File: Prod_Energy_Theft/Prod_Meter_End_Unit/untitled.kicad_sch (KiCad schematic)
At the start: 11 parts, among them J5 Screw_Terminal_01x02, J9 Screw_Terminal_01x02, K2 Relay_DPST_Latching_2coil, Q3 AO3400A, Q4 AO3400A

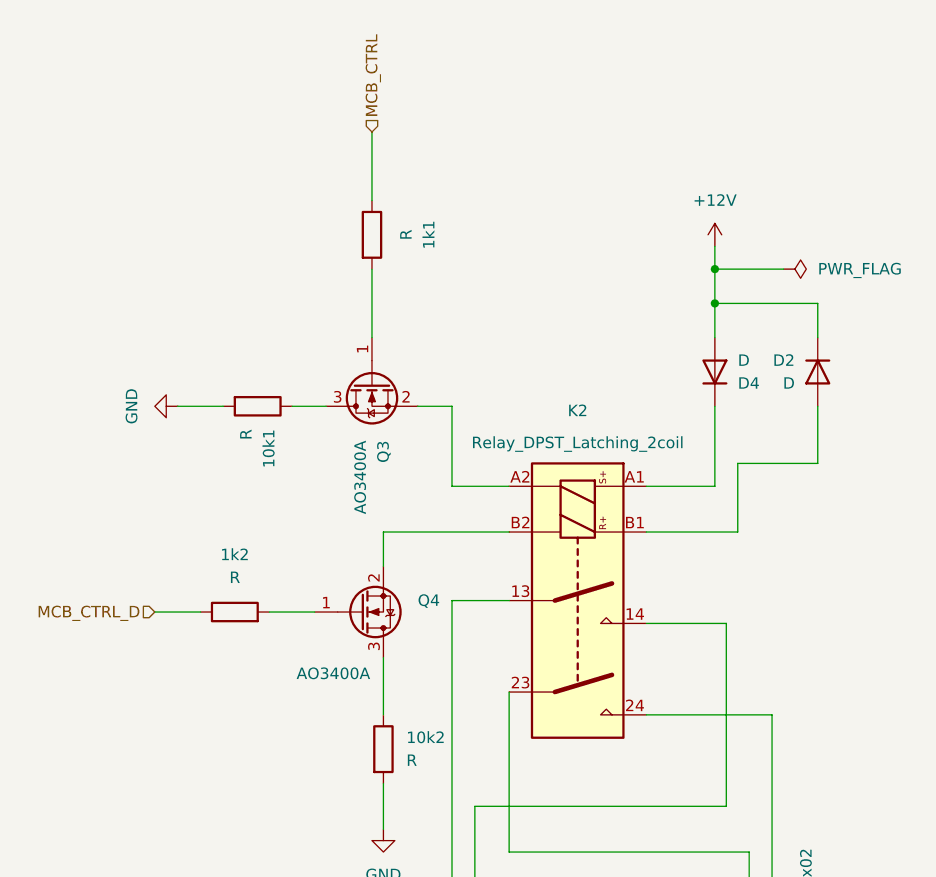
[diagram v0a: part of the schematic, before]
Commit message: Chnages in power and ADE7816
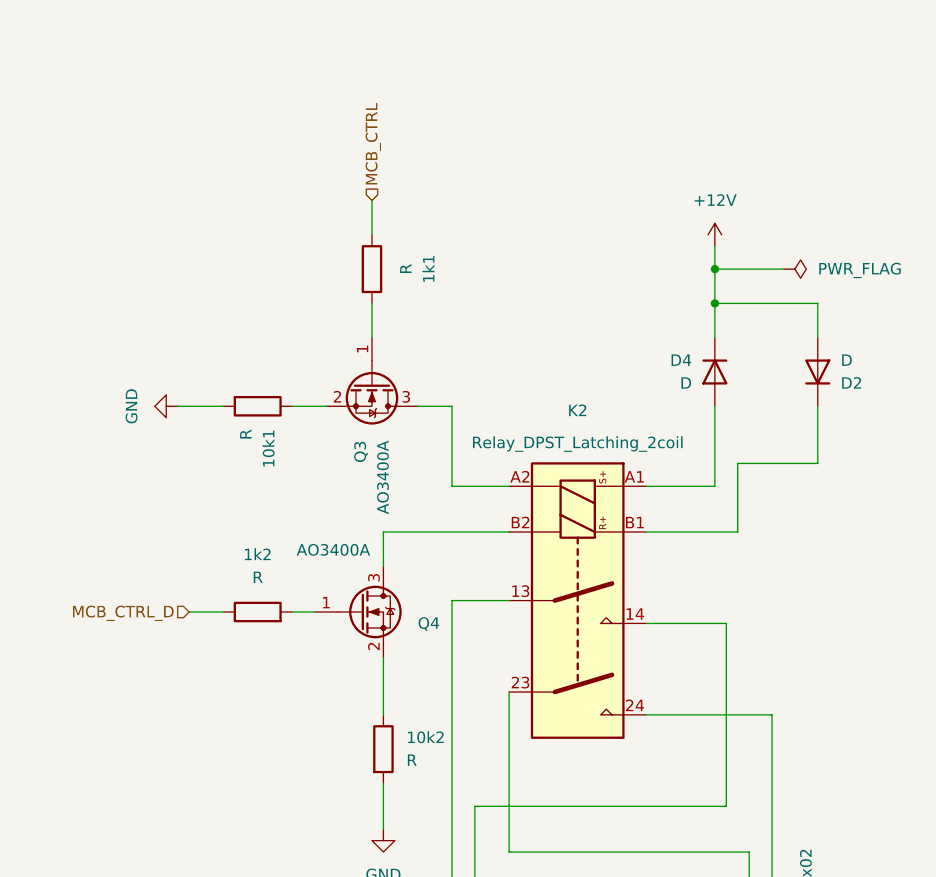
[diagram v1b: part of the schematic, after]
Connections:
- net +12V: now also D2.2 (A), D4.1 (K); no longer D2.1 (K), D4.2 (A)
- net at K2.A1: now also D4.2 (A); no longer D4.1 (K)
- net at K2.A2: now also Q3.3 (D); no longer Q3.2 (S)
- net at K2.B1: now also D2.1 (K); no longer D2.2 (A)
- net at K2.B2: now also Q4.3 (D); no longer Q4.2 (S)
- net at 10k2.1: now also Q4.2 (S); no longer Q4.3 (D)
- net at 10k1.1: now also Q3.2 (S); no longer Q3.3 (D)
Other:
- moved on the sheet: 1k1, 1k2, D2, D4, Q3
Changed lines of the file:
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@@
 	(wire
 		(pts
-			(xy 116.84 72.39) (xy 116.84 80.01)
+			(xy 116.84 76.2) (xy 116.84 80.01)
 		)
 		(stroke
@@
 	(wire
 		(pts
-			(xy 111.76 87.63) (xy 107.95 87.63)
-		)
-		(stroke
-			(width 0)
-			(type default)
-		)
-	)
-	(wire
-		(pts
-			(xy 105.41 110.49) (xy 110.49 110.49)
+			(xy 107.95 110.49) (xy 110.49 110.49)
 		)
 		(stroke
@@
 	(wire
 		(pts
+			(xy 118.11 115.57) (xy 118.11 121.92)
+		)
+		(stroke
+			(width 0)
+			(type default)
+		)
+	)
+	(wire
+		(pts
 			(xy 154.94 69.85) (xy 154.94 72.39)
 		)
@@
 	(wire
 		(pts
-			(xy 118.11 121.92) (xy 118.11 115.57)
-		)
-		(stroke
-			(width 0)
-			(type default)
-		)
-	)
-	(wire
-		(pts
 			(xy 100.33 87.63) (xy 95.25 87.63)
 		)
@@
 	(wire
 		(pts
-			(xy 116.84 57.15) (xy 116.84 64.77)
+			(xy 116.84 64.77) (xy 116.84 68.58)
 		)
 		(stroke
@@
 	(wire
 		(pts
+			(xy 107.95 87.63) (xy 111.76 87.63)
+		)
+		(stroke
+			(width 0)
+			(type default)
+		)
+	)
+	(wire
+		(pts
 			(xy 147.32 121.92) (xy 161.29 121.92)
 		)
@@
 	(wire
 		(pts
-			(xy 92.71 110.49) (xy 97.79 110.49)
+			(xy 96.52 110.49) (xy 100.33 110.49)
 		)
 		(stroke
@@
 	(wire
 		(pts
+			(xy 147.32 96.52) (xy 154.94 96.52)
+		)
+		(stroke
+			(width 0)
+			(type default)
+		)
+	)
+	(wire
+		(pts
+			(xy 154.94 87.63) (xy 154.94 96.52)
+		)
+		(stroke
+			(width 0)
+			(type default)
+		)
+	)
+	(wire
+		(pts
+			(xy 132.08 109.22) (xy 125.73 109.22)
+		)
+		(stroke
+			(width 0)
+			(type default)
+		)
+	)
+	(wire
+		(pts
+			(xy 166.37 93.98) (xy 166.37 87.63)
+		)
+		(stroke
+			(width 0)
+			(type default)
+		)
+	)
+	(wire
+		(pts
 			(xy 121.92 87.63) (xy 125.73 87.63)
-		)
-		(stroke
-			(width 0)
-			(type default)
-		)
-	)
-	(wire
-		(pts
-			(xy 147.32 96.52) (xy 154.94 96.52)
-		)
-		(stroke
-			(width 0)
-			(type default)
-		)
-	)
-	(wire
-		(pts
-			(xy 154.94 87.63) (xy 154.94 96.52)
-		)
-		(stroke
-			(width 0)
-			(type default)
-		)
-	)
-	(wire
-		(pts
-			(xy 132.08 109.22) (xy 125.73 109.22)
-		)
-		(stroke
-			(width 0)
-			(type default)
-		)
-	)
-	(wire
-		(pts
-			(xy 166.37 93.98) (xy 166.37 87.63)
 		)
 		(stroke
@@
 	(hierarchical_label "MCB_CTRL"
 		(shape input)
-		(at 116.84 57.15 90)
+		(at 116.84 64.77 90)
 		(effects
 			(font
@@
 	(hierarchical_label "MCB_CTRL_D"
 		(shape input)
-		(at 92.71 110.49 180)
+		(at 96.52 110.49 180)
 		(effects
 			(font
@@
 	(symbol
 		(lib_id "Device:D")
-		(at 154.94 83.82 270)
+		(at 154.94 83.82 90)
 		(mirror x)
 		(unit 1)
@@
 		(dnp no)
 		(property "Reference" "D4"
-			(at 157.48 85.0901 90)
+			(at 152.4 82.5499 90)
 			(effects
 				(font
@@
 		)
 		(property "Value" "D"
-			(at 157.48 82.5501 90)
+			(at 152.4 85.0899 90)
 			(effects
 				(font
@@
 	(symbol
 		(lib_id "Device:R")
-		(at 116.84 68.58 0)
+		(at 116.84 72.39 0)
 		(unit 1)
 		(exclude_from_sim no)
@@
 		(fields_autoplaced yes)
 		(property "Reference" "1k1"
-			(at 123.19 68.58 90)
+			(at 123.19 72.39 90)
 			(effects
 				(font
@@
 		)
 		(property "Value" "R"
-			(at 120.65 68.58 90)
+			(at 120.65 72.39 90)
 			(effects
 				(font
@@
 		)
 		(property "Footprint" "Resistor_SMD:R_0805_2012Metric"
-			(at 115.062 68.58 90)
+			(at 115.062 72.39 90)
 			(effects
 				(font
@@
 		)
 		(property "Datasheet" "~"
-			(at 116.84 68.58 0)
+			(at 116.84 72.39 0)
 			(effects
 				(font
@@
 		)
 		(property "Description" "Resistor"
-			(at 116.84 68.58 0)
+			(at 116.84 72.39 0)
 			(effects
 				(font
@@
 		(lib_id "Transistor_FET:AO3400A")
 		(at 115.57 110.49 0)
-		(mirror x)
 		(unit 1)
 		(exclude_from_sim no)
@@
 		(dnp no)
 		(property "Reference" "Q4"
-			(at 121.92 109.2199 0)
+			(at 121.92 111.7601 0)
 			(effects
 				(font
@@
 		)
 		(property "Value" "AO3400A"
-			(at 108.458 117.348 0)
+			(at 108.458 103.632 0)
 			(effects
 				(font
@@
 		)
 		(property "Footprint" "Package_TO_SOT_SMD:SOT-23"
-			(at 120.65 108.585 0)
+			(at 120.65 112.395 0)
 			(effects
 				(font
@@
 		)
 		(property "Datasheet" "http://www.aosmd.com/pdfs/datasheet/AO3400A.pdf"
-			(at 120.65 106.68 0)
+			(at 120.65 114.3 0)
 			(effects
 				(font
@@
 	(symbol
 		(lib_id "Transistor_FET:AO3400A")
-		(at 116.84 85.09 90)
-		(mirror x)
+		(at 116.84 85.09 270)
 		(unit 1)
 		(exclude_from_sim no)
@@
 		(dnp no)
 		(property "Reference" "Q3"
-			(at 118.1101 91.44 0)
+			(at 115.5699 91.44 0)
 			(effects
 				(font
@@
 		)
 		(property "Value" "AO3400A"
-			(at 115.5701 91.44 0)
+			(at 118.1099 91.44 0)
 			(effects
 				(font
@@
 		)
 		(property "Footprint" "Package_TO_SOT_SMD:SOT-23"
-			(at 118.745 90.17 0)
+			(at 114.935 90.17 0)
 			(effects
 				(font
@@
 		)
 		(property "Datasheet" "http://www.aosmd.com/pdfs/datasheet/AO3400A.pdf"
-			(at 120.65 90.17 0)
+			(at 113.03 90.17 0)
 			(effects
 				(font
@@
 	(symbol
 		(lib_id "Device:R")
-		(at 101.6 110.49 90)
+		(at 104.14 110.49 90)
 		(unit 1)
 		(exclude_from_sim no)
@@
 		(fields_autoplaced yes)
 		(property "Reference" "1k2"
-			(at 101.6 104.14 90)
+			(at 104.14 104.14 90)
 			(effects
 				(font
@@
 		)
 		(property "Value" "R"
-			(at 101.6 106.68 90)
+			(at 104.14 106.68 90)
 			(effects
 				(font
@@
 		)
 		(property "Footprint" "Resistor_SMD:R_0805_2012Metric"
-			(at 101.6 112.268 90)
+			(at 104.14 112.268 90)
 			(effects
 				(font
@@
 		)
 		(property "Datasheet" "~"
-			(at 101.6 110.49 0)
+			(at 104.14 110.49 0)
 			(effects
 				(font
@@
 		)
 		(property "Description" "Resistor"
-			(at 101.6 110.49 0)
+			(at 104.14 110.49 0)
 			(effects
 				(font
@@
 	(symbol
 		(lib_id "Device:D")
-		(at 166.37 83.82 90)
+		(at 166.37 83.82 270)
 		(mirror x)
 		(unit 1)
@@
 		(dnp no)
 		(property "Reference" "D2"
-			(at 163.83 82.5499 90)
+			(at 168.91 85.0901 90)
 			(effects
 				(font
@@
 		)
 		(property "Value" "D"
-			(at 163.83 85.0899 90)
-			(effects
-				(font
+			(at 168.91 82.5501 90)
+			(effects
+				(font

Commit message: PCB
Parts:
- removed 10k1, 10k2, 1k1, 1k2: R, Resistor_SMD:R_0805_2012Metric, symbol Device:R
- removed D2, D4: D, Diode_SMD:D_SOD-123, symbol Device:D
- removed J5, J9: Screw_Terminal_01x02, TerminalBlock_Phoenix:TerminalBlock_Phoenix_PTSM-0,5-2-2,5-V-SMD_1x02-1MP_P2.50mm_Vertical, symbol Connector:Screw_Terminal_01x02
- removed K2: Relay_DPST_Latching_2coil, symbol Relay:Relay_DPST_Latching_2coil
- removed Q3, Q4: AO3400A, Package_TO_SOT_SMD:SOT-23, symbol Transistor_FET:AO3400A
- added 10k3, 10k4, 1k3, 1k4: R, Resistor_SMD:R_0805_2012Metric, symbol Device:R
- added C3: 100uf, Capacitor_SMD:C_0805_2012Metric, symbol Device:C
- added D11, D12: D, Diode_SMD:D_SOD-123, symbol Device:D
- added J12, J13: Screw_Terminal_01x02, TerminalBlock_Phoenix:TerminalBlock_Phoenix_MKDS-1,5-2-5.08_1x02_P5.08mm_Horizontal, symbol Connector:Screw_Terminal_01x02
- added K1: HFD2/012-S-L2-D, theftdetection:RELAY10_HFD2&slash_012_HNG, symbol 2026-03-04_10-29-55:HFD2_012-S-L2-D
- added Q5, Q6: AO3400A, Package_TO_SOT_SMD:SOT-23, symbol Transistor_FET:AO3400A
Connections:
- net +12V: now also C3.1, D11.1 (K), D12.2 (A), K1.1, K1.2
- net GND: now also 10k3.2, 10k4.2, C3.2
- new net: 10k4.1, Q6.2 (S)
- new net: 1k3.2, Q5.1 (G)
- new net: 1k4.2, Q6.1 (G)
- new net: J13.1 (Pin_1), K1.13
- new net: J12.1 (Pin_1), K1.4
- new net: J12.2 (Pin_2), K1.8
- new net: J13.2 (Pin_2), K1.9
- new net: 10k3.1, Q5.2 (S)
- new net MCB_RESET: 1k4.1
- new net MCB_SET: 1k3.1
- new net RELAY_RESET: D12.1 (K), K1.15, Q6.3 (D)
- new net RELAY_SET: D11.2 (A), K1.16, Q5.3 (D)
- no-connect marks 0 -> 2

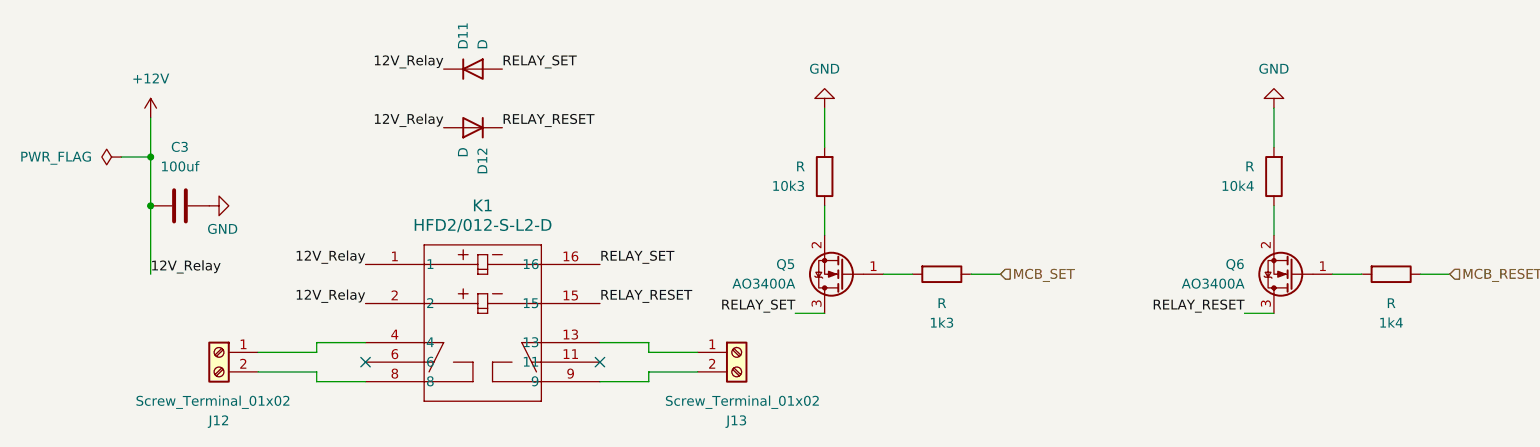
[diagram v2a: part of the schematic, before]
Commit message: update in BOM list
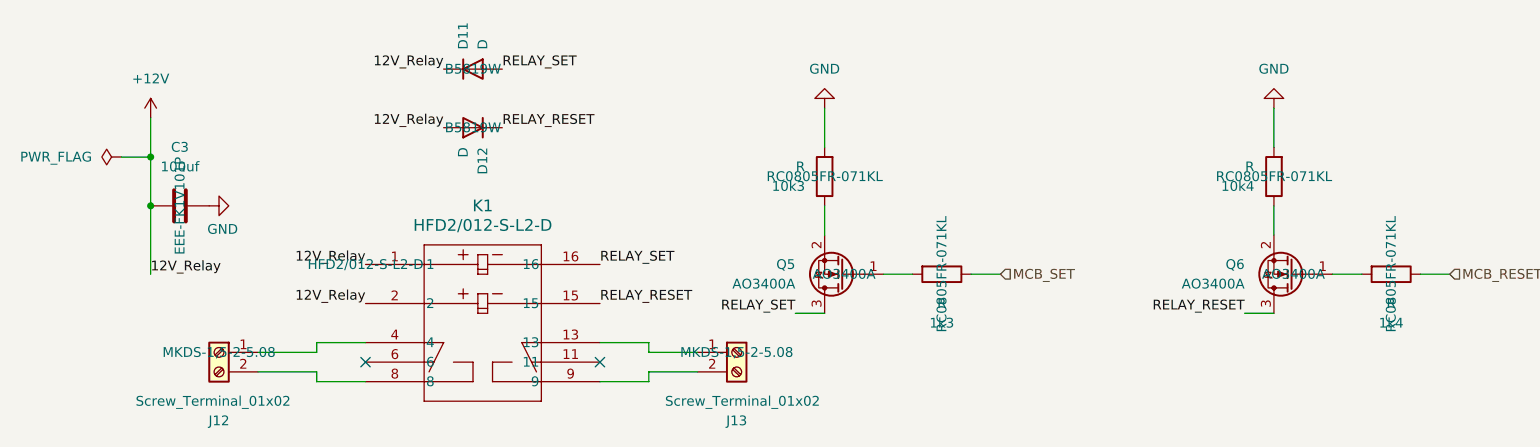
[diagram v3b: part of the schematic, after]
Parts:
- 10k3, 10k4, 1k3, 1k4: Part Number (none) -> RC0805FR-071KL
- C3: Part Number (none) -> EEE-FK1V101P
- D11, D12: Part Number (none) -> B5819W
- J12, J13: Part Number (none) -> MKDS-1,5-2-5.08
- K1: Part Number (none) -> HFD2/012-S-L2-D
- Q5, Q6: Part Number (none) -> AO3400A
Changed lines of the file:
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@@
+			)
+		)
+		(property "Part Number" "RC0805FR-071KL "
+			(at 234.95 93.98 0)
+			(effects
+				(font
+					(size 1.27 1.27)
+				)
 			)
 		)
@@
 			)
 		)
+		(property "Part Number" "RC0805FR-071KL "
+			(at 191.77 106.68 0)
+			(effects
+				(font
+					(size 1.27 1.27)
+				)
+			)
+		)
 		(pin "2"
 		)
@@
 				)
 				(hide yes)
+			)
+		)
+		(property "Part Number" "AO3400A "
+			(at 237.49 106.68 0)
+			(effects
+				(font
+					(size 1.27 1.27)
+				)
 			)
 		)
@@
 			)
 		)
+		(property "Part Number" "RC0805FR-071KL "
+			(at 250.19 106.68 0)
+			(effects
+				(font
+					(size 1.27 1.27)
+				)
+			)
+		)
 		(pin "2"
 		)
@@
 			)
 		)
+		(property "Part Number" "B5819W "
+			(at 130.81 80.01 0)
+			(effects
+				(font
+					(size 1.27 1.27)
+				)
+			)
+		)
 		(pin "1"
 		)
@@
 			)
 		)
+		(property "Part Number" "HFD2/012-S-L2-D "
+			(at 116.84 105.41 0)
+			(effects
+				(font
+					(size 1.27 1.27)
+				)
+			)
+		)
 		(pin "15"
 		)
@@
 			)
 		)
+		(property "Part Number" "MKDS-1,5-2-5.08 "
+			(at 97.79 116.84 0)
+			(effects
+				(font
+					(size 1.27 1.27)
+				)
+			)
+		)
 		(pin "2"
 		)
@@
 				)
 				(hide yes)
+			)
+		)
+		(property "Part Number" "MKDS-1,5-2-5.08 "
+			(at 165.1 116.84 0)
+			(effects
+				(font
+					(size 1.27 1.27)
+				)
 			)
 		)
@@
 			)
 		)
+		(property "Part Number" "RC0805FR-071KL "
+			(at 176.53 93.98 0)
+			(effects
+				(font
+					(size 1.27 1.27)
+				)
+			)
+		)
 		(pin "2"
 		)
@@
 			)
 		)
+		(property "Part Number" "EEE-FK1V101P "
+			(at 92.71 97.79 0)
+			(effects
+				(font
+					(size 1.27 1.27)
+				)
+			)
+		)
 		(pin "1"
 		)
@@
 			)
 		)
+		(property "Part Number" "AO3400A "
+			(at 179.07 106.68 0)
+			(effects
+				(font
+					(size 1.27 1.27)
+				)
+			)
+		)
 		(pin "2"
 		)
@@
 			)
 		)
+		(property "Part Number" "B5819W "
+			(at 130.81 87.63 0)
+			(effects
+				(font
+					(size 1.27 1.27)
+				)
+			)
+		)
